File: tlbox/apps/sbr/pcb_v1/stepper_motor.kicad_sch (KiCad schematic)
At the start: 1 part

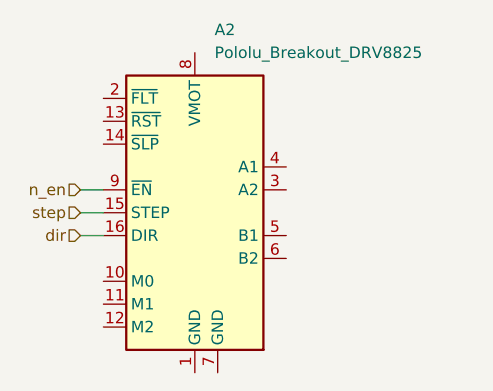
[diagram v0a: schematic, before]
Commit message: update kicad v10
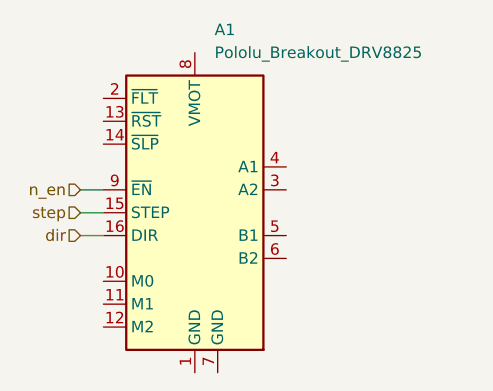
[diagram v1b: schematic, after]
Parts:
- renumbered A2 to A1
